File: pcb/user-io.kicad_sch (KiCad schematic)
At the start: 17 parts, among them J4 FH26-15S-0.3SHW(05), SW2 PEC12R-4222F-S0024, U150 SN74LVC1G14DBVR

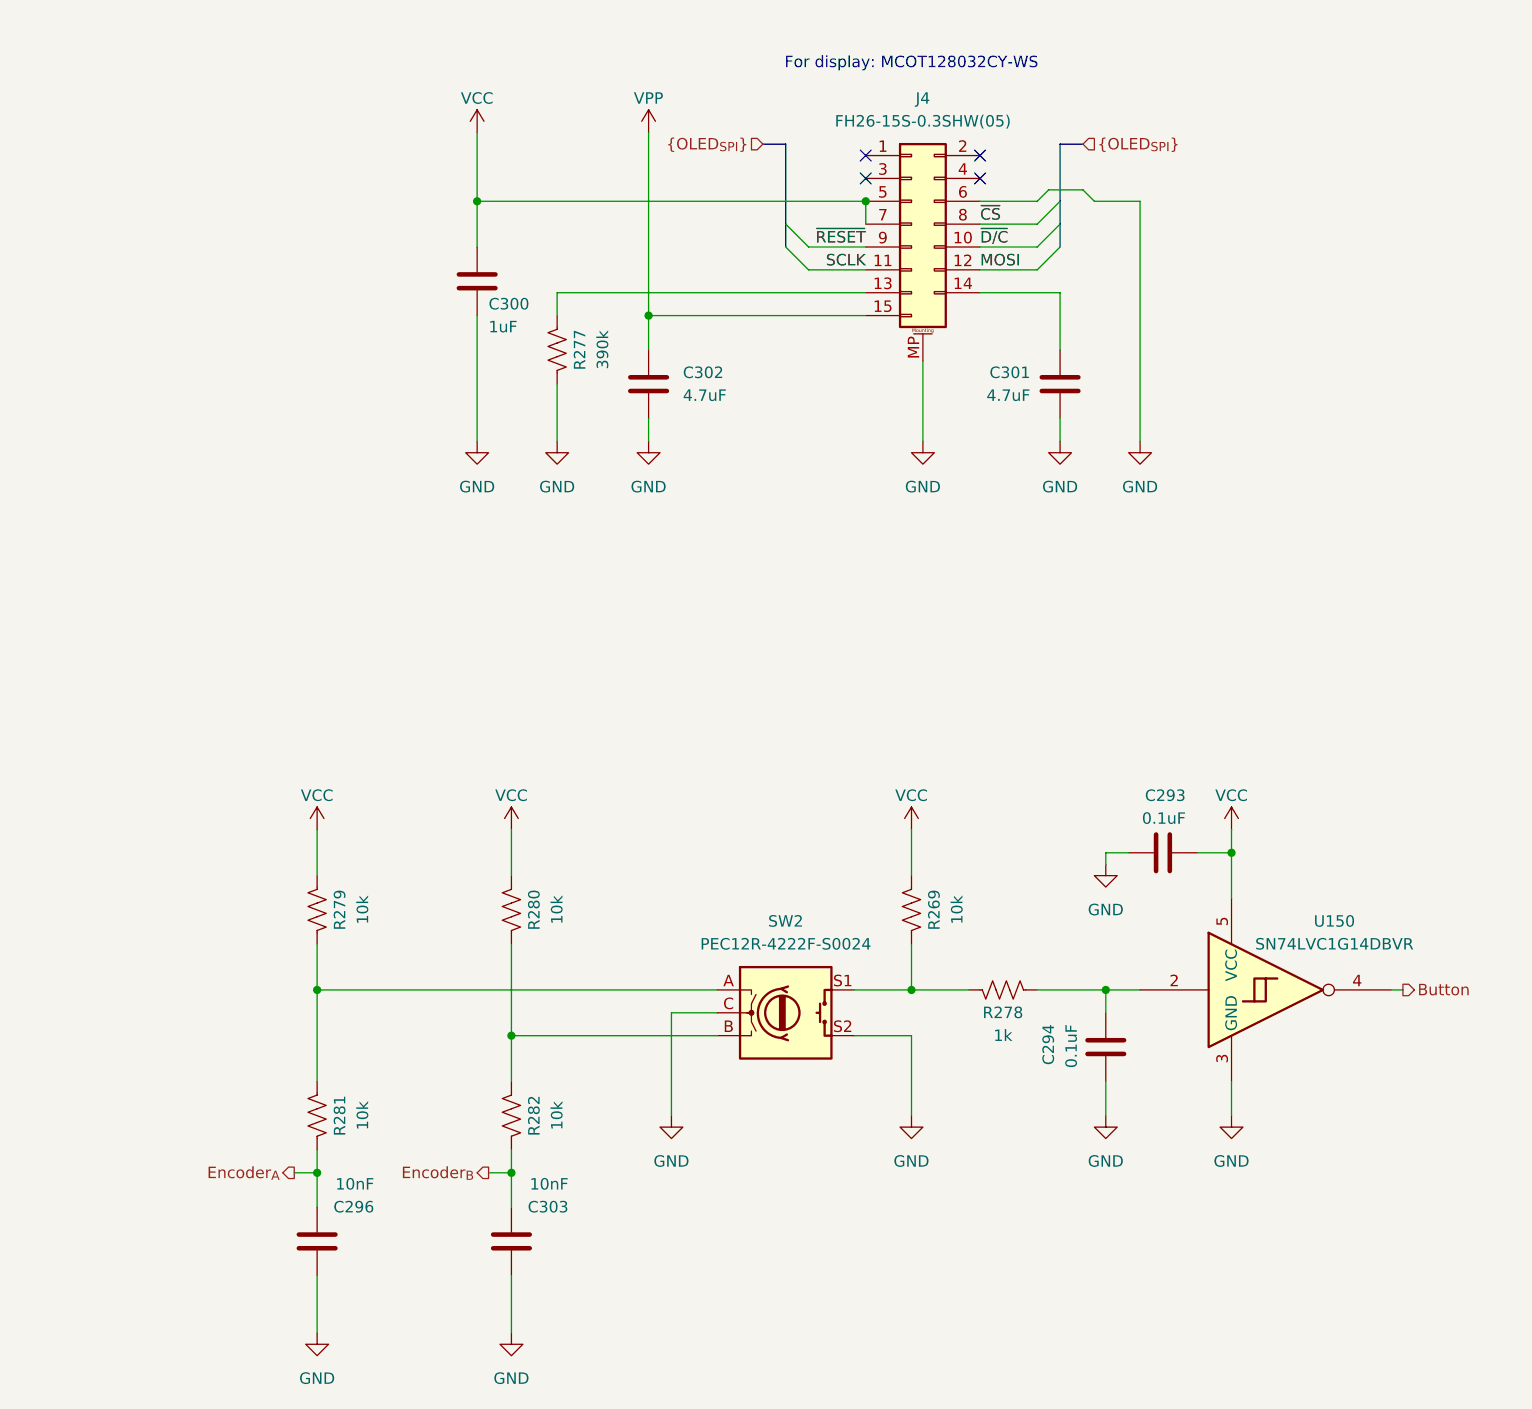
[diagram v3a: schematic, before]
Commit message: Routing nearly complete
- Power switch is too tall I think
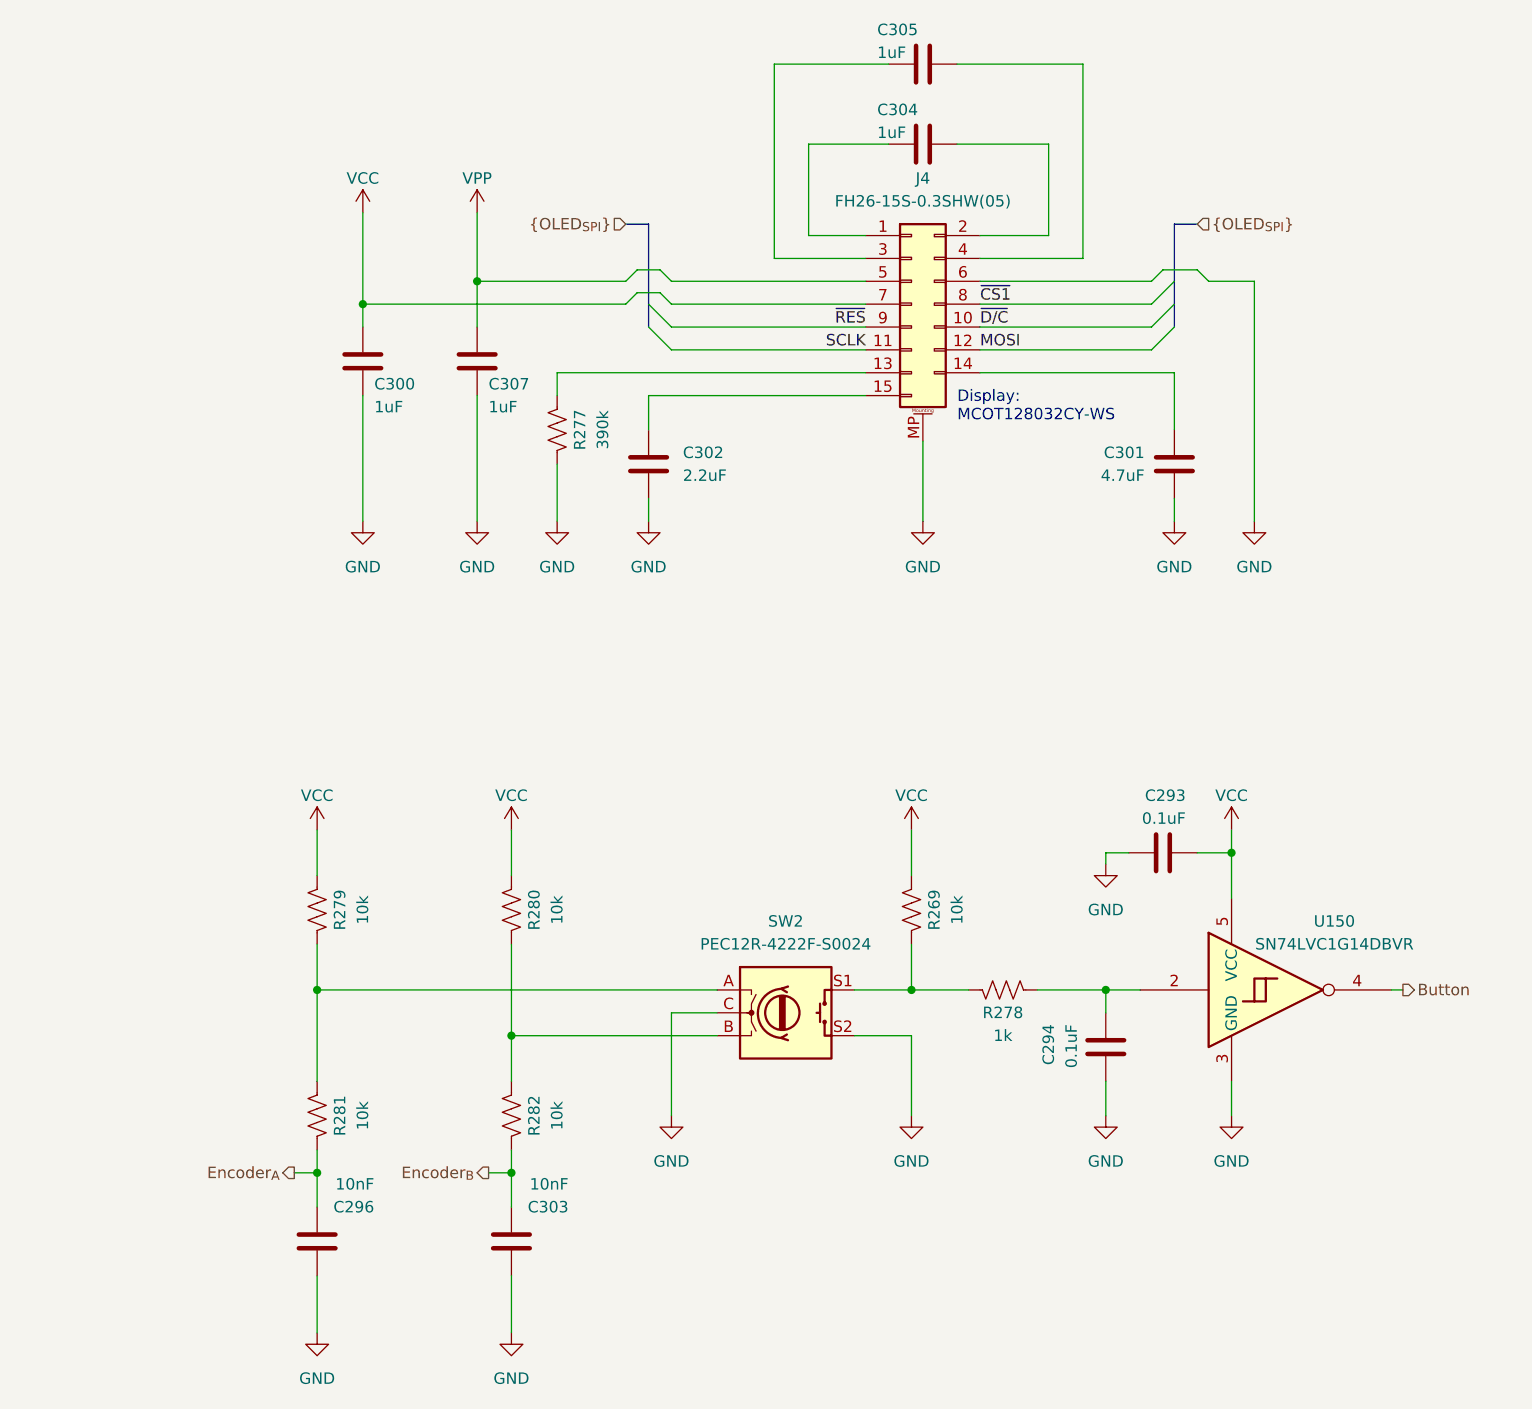
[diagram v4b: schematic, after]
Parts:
- added C304, C305, C307: 1uF, Capacitor_SMD:C_0603_1608Metric, symbol Device:C
- C293, C294, C296, C303: TempCo (none) -> X7R
- C300: TempCo (none) -> X5R; Voltage (none) -> 16V
- C301: footprint Capacitor_SMD:C_0805_2012Metric -> Capacitor_SMD:C_1206_3216Metric; TempCo (none) -> X7R; Voltage (none) -> 16V
- C302: value 4.7uF -> 2.2uF; TempCo (none) -> X5R; Voltage (none) -> 16V
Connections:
- net GND: now also C307.2
- net VCC: no longer J4.5 (Pin_5)
- net VPP: now also J4.5 (Pin_5), C307.1; no longer C302.1, J4.15 (Pin_15)
- net at J4.1 (Pin_1): now also C304.1
- net at J4.2 (Pin_2): now also C304.2
- net at J4.3 (Pin_3): now also C305.1
- net at J4.4 (Pin_4): now also C305.2
- net ~{CS} renamed ~{CS1}
- net ~{RESET} renamed ~{RES}
- new net: C302.1, J4.15 (Pin_15)
- no-connect marks 4 -> 0
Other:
- note added: "Display: MCOT128032CY-WS"
- note removed: "For display: MCOT128032CY-WS"
- moved on the sheet: C300, C301, C302, J4, R277

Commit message: Fix MCP73831 subcircuit
- Add decoupling capacitor on Vbat
- Add more thermal support to layout (solid connection of ground to
  ground plane copper and addition of thermal vias)
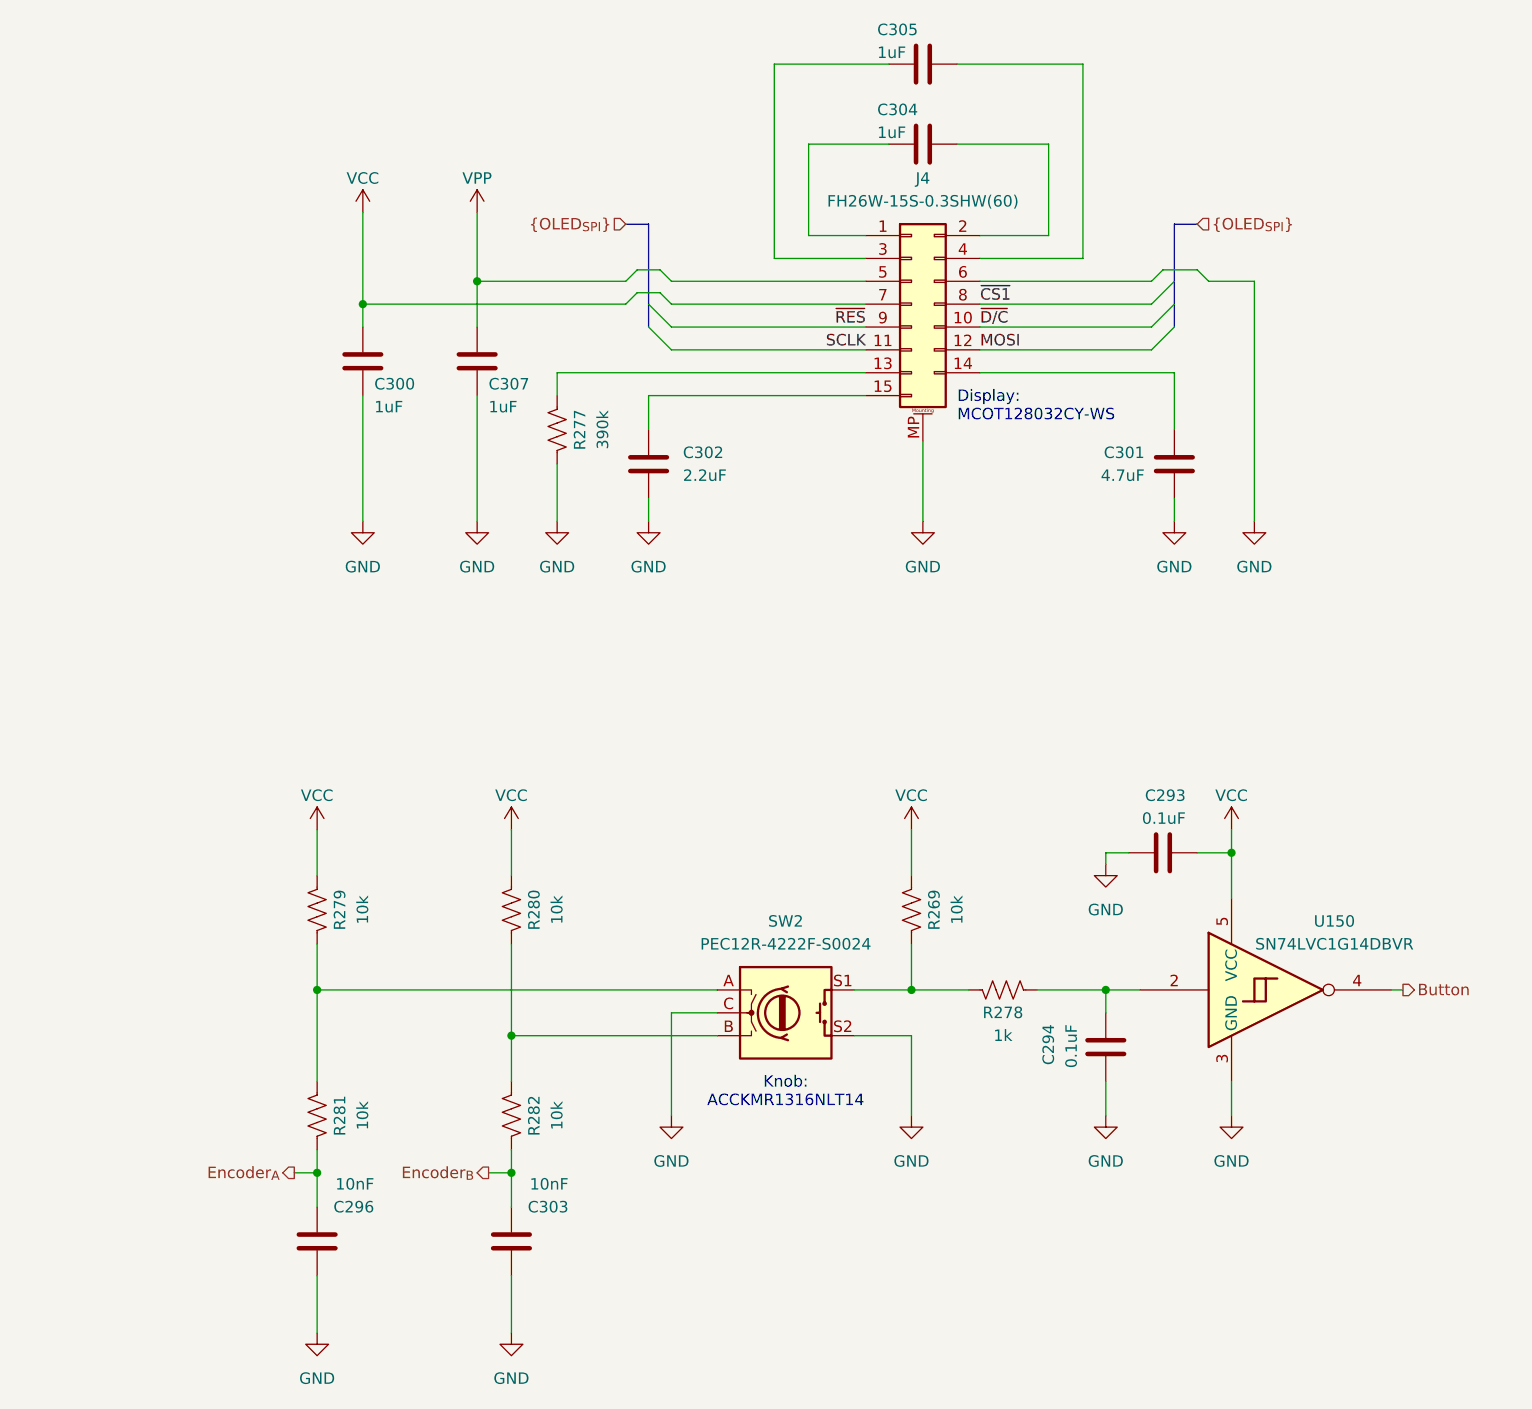
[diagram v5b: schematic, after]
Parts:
- J4: value FH26-15S-0.3SHW(05) -> FH26W-15S-0.3SHW(60)
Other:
- note added: "Knob: ACCKMR1316NLT14"
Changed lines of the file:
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@@
 	(paper "A4")
 	(title_block
-		(rev "A")
+		(rev "B")
 		(comment 1 "Jonathan P. Newman")
 	)
@@
 			)
 			(justify left)
+		)
+	)
+	(text "Knob:\nACCKMR1316NLT14"
+		(exclude_from_sim no)
+		(at 139.7 142.24 0)
+		(effects
+			(font
+				(size 1.27 1.27)
+			)
 		)
 	)
@@
 			)
 		)
-		(property "Value" "FH26-15S-0.3SHW(05)"
+		(property "Value" "FH26W-15S-0.3SHW(60)"
 			(at 154.94 43.18 0)
 			(effects

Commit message: Address several issues found when testing rev. A
- Add Reset button to back panel
- Make board smaller
- Move battery to bottom of device
- Replace OLED with a more reasonable choice.
- Etc.
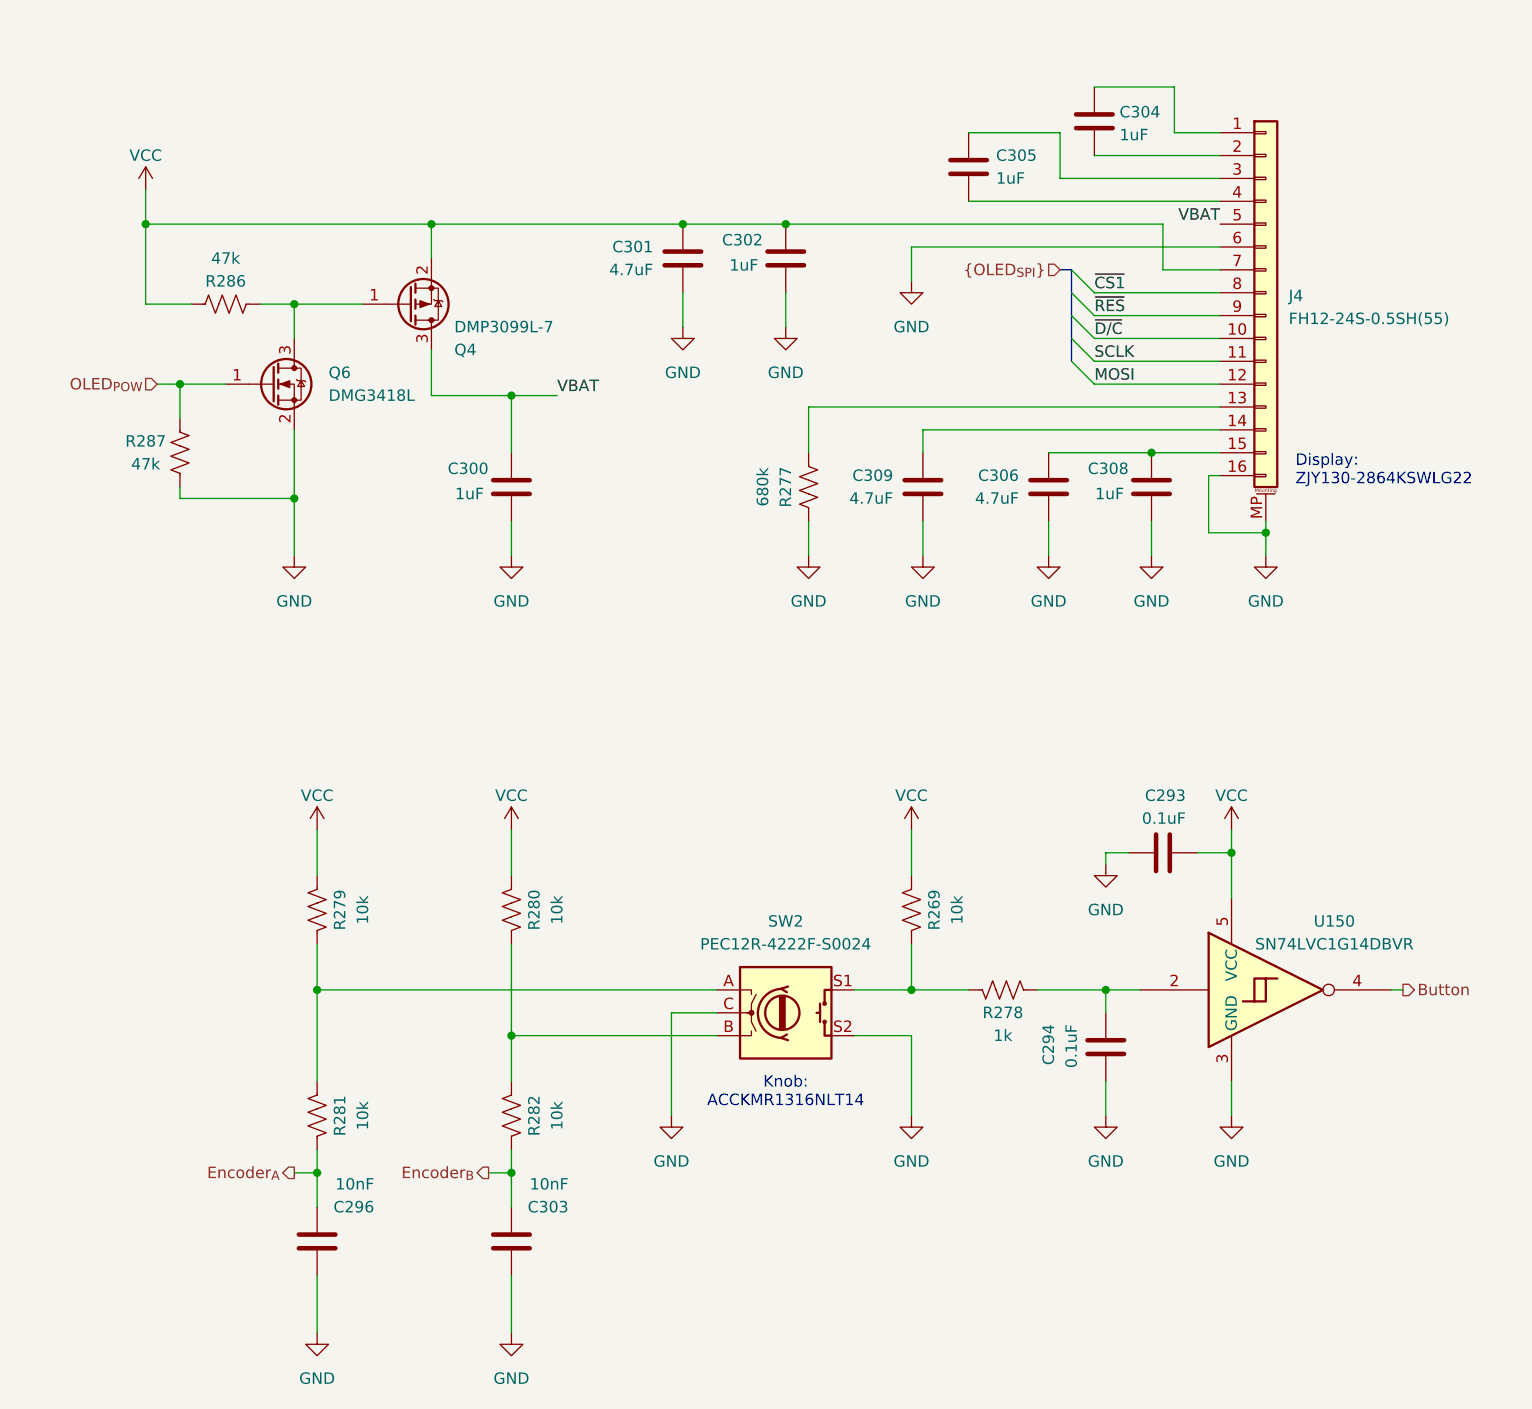
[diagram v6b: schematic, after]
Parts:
- removed C307: 1uF, Capacitor_SMD:C_0603_1608Metric, symbol Device:C
- removed J4: FH26W-15S-0.3SHW(60), Connector_FFC-FPC:Hirose_FH26-15S-0.3SHW_2Rows-15Pins-1MP_P0.60mm_Horizontal, symbol Connector_Generic_MountingPin:Conn_2Rows-15Pins_MountingPin
- added C306, C309: 4.7uF, Capacitor_SMD:C_1206_3216Metric, symbol Device:C
- added C308: 1uF, Capacitor_SMD:C_0603_1608Metric, symbol Device:C
- added J4: FH12-24S-0.5SH(55), Connector_FFC-FPC:Hirose_FH12-16S-0.5SH_1x16-1MP_P0.50mm_Horizontal, symbol Connector_Generic_MountingPin:Conn_01x16_MountingPin
- added Q4: DMP3099L-7, Package_TO_SOT_SMD:SOT-23, symbol Transistor_FET:DMG2301L
- added Q6: DMG3418L, Package_TO_SOT_SMD:SOT-23, symbol Transistor_FET:DMG3414U
- added R286, R287: 47k, Resistor_SMD:R_0402_1005Metric, symbol Device:R_US
- C302: value 2.2uF -> 1uF; footprint Capacitor_SMD:C_0805_2012Metric -> Capacitor_SMD:C_0603_1608Metric
- R277: value 390k -> 680k
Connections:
- net GND: now also C300.1, C302.1, C306.2, C308.1, C309.2, J4.16 (Pin_16), J4.6 (Pin_6), J4.MP (MountPin), Q6.2 (S), R287.2; no longer C300.2, C302.2
- net MOSI: now also J4.12 (Pin_12)
- net SCLK: now also J4.11 (Pin_11)
- net VCC: now also C301.1, C302.2, J4.7 (Pin_7), Q4.2 (S), R286.2; no longer C300.1
- net ~{CS1}: now also J4.8 (Pin_8)
- net ~{D/C}: now also J4.10 (Pin_10)
- net ~{RES}: now also J4.9 (Pin_9)
- net at R277.1: now also J4.13 (Pin_13)
- net at C304.1: now also J4.2 (Pin_2)
- net at C304.2: now also J4.1 (Pin_1)
- net at C305.1: now also J4.4 (Pin_4)
- net at C305.2: now also J4.3 (Pin_3)
- new net: Q4.1 (G), Q6.3 (D), R286.1
- new net: C306.1, C308.2, J4.15 (Pin_15)
- new net: C309.1, J4.14 (Pin_14)
- new net OLED_{POW}: Q6.1 (G), R287.1
- new net VBAT: C300.2, J4.5 (Pin_5), Q4.3 (D)
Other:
- note added: "Display: ZJY130-2864KSWLG22"
- note removed: "Display: MCOT128032CY-WS"
- moved on the sheet: C304, C305
